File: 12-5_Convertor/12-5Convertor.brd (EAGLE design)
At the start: 29.1 x 41.3 mm, 14 parts, among them U1 LM2678

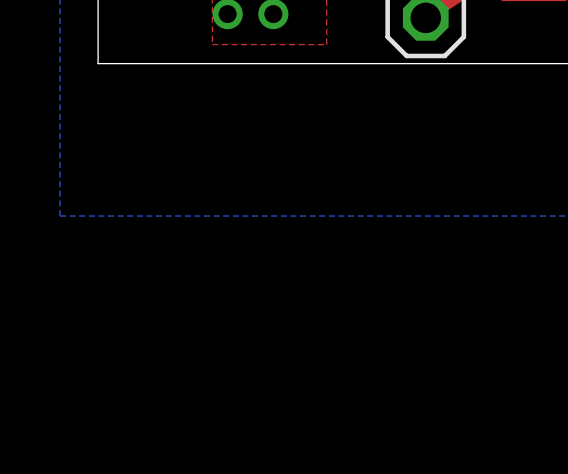
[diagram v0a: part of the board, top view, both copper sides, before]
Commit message: Update the buck regulator.
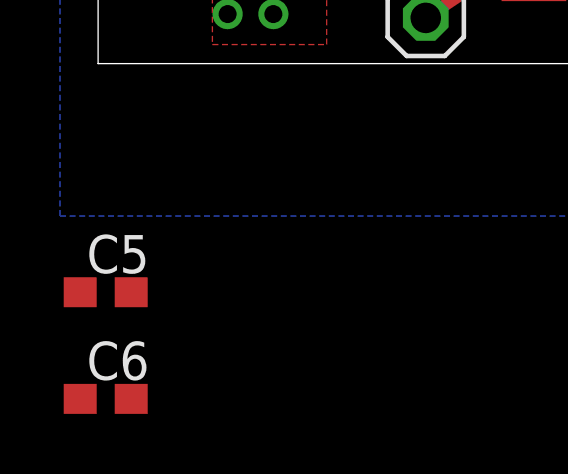
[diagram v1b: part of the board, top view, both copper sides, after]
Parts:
- added C5, C6: (no value), eagle-ltspice:C0603
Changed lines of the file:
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@@
 <?xml version="1.0" encoding="utf-8"?>
 <!DOCTYPE eagle SYSTEM "eagle.dtd">
-<eagle version="7.3.0">
+<eagle version="7.4.0">
 <drawing>
 <settings>
@@
 <attribute name="NAME" x="33.186" y="30.87" size="1.27" layer="21"/>
 </element>
+<element name="C5" library="eagle-ltspice" package="C0603" value="" x="32.004" y="10.16">
+<attribute name="SPICEMODEL" value="NONE" x="32.004" y="10.16" size="1.778" layer="27" display="off"/>
+<attribute name="SPICEPREFIX" value="C" x="32.004" y="10.16" size="1.778" layer="27" display="off"/>
+</element>
+<element name="C6" library="eagle-ltspice" package="C0603" value="" x="32.004" y="6.604">
+<attribute name="SPICEMODEL" value="NONE" x="32.004" y="6.604" size="1.778" layer="27" display="off"/>
+<attribute name="SPICEPREFIX" value="C" x="32.004" y="6.604" size="1.778" layer="27" display="off"/>
+</element>
 </elements>

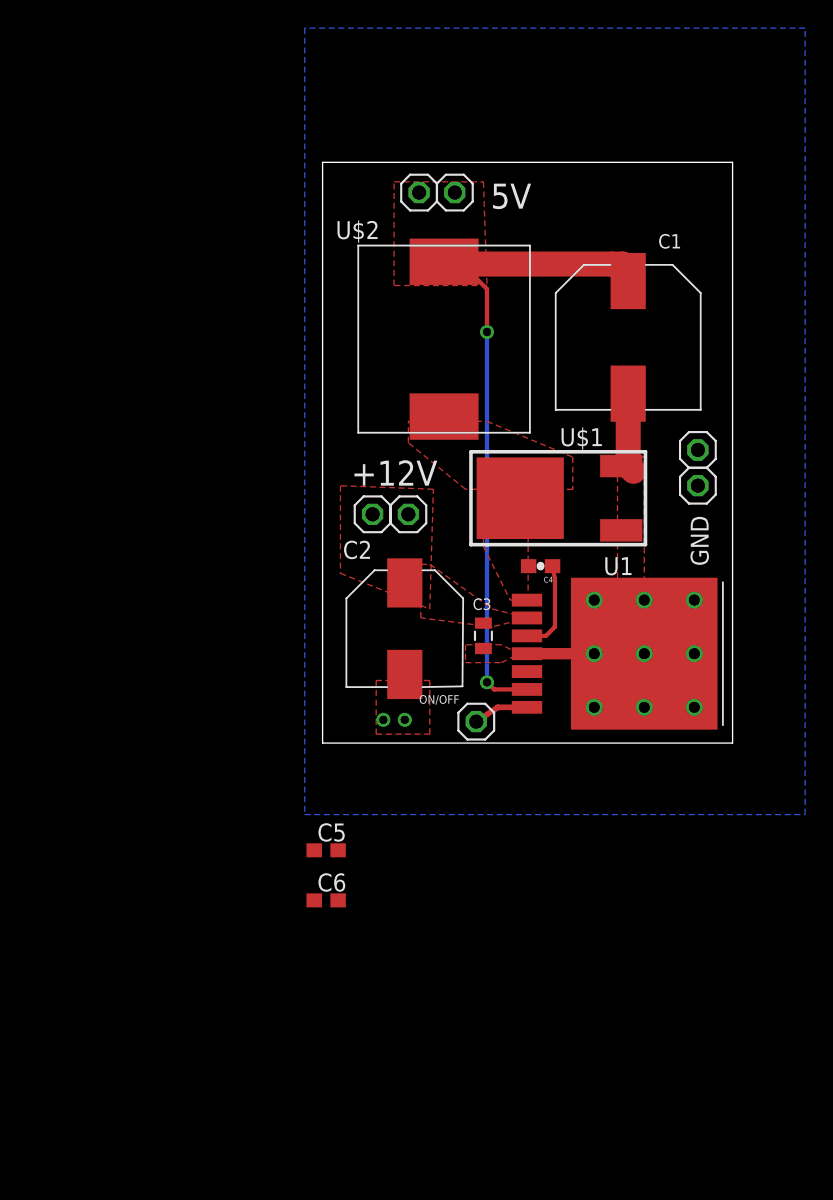
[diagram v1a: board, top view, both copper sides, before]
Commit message: Fixed labels. Added linear regulator and current sensor
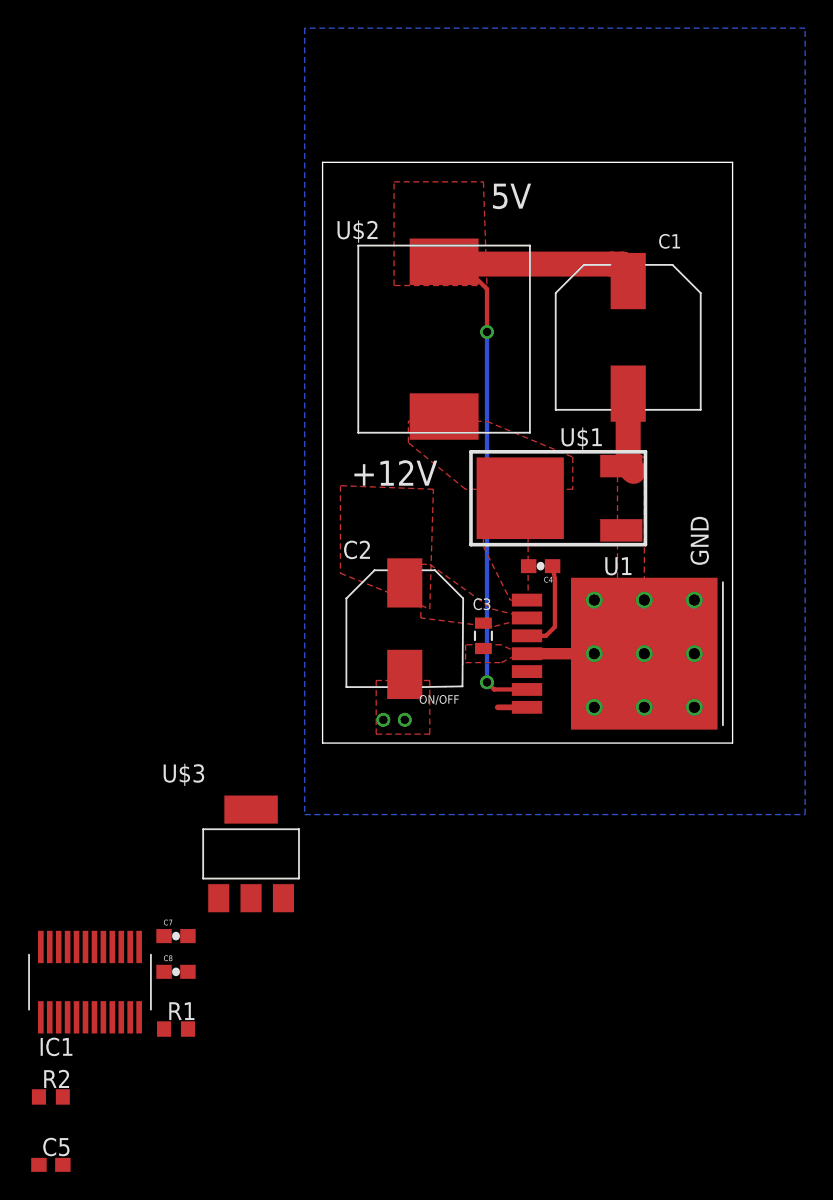
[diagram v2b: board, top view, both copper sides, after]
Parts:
- removed C6: (no value), eagle-ltspice:C0603
- removed JP1, JP2, JP3, JP4, JP5, JP6, JP7: (no value), pinhead:1X01
- added C7, C8: 10UF, SparkFun-Passives:0603-CAP
- added IC1: ACS764, ACS764:SSOP24
- added R1: 1kOhm, DiscreteComponents:R0603
- added R2: 10kOhm, DiscreteComponents:R0603
- added U$3: NCP1117, PowerComponents:NCP1117
- C2: value C-ALUMINUM(47UF) -> 47UF
- C5: value (none) -> 0.1uF
- moved C5 29.7 mm to (12.4, -12.2)
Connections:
- removed net ON/OFF: JP4.1, U1.7
- new net +3V3: C5.1, IC1.8, R1.2, R2.2, U1.7
- new net FAULT: IC1.15, R2.1
- new net N$1: C8.1, R1.1, U$3.OUT
- new net N$10: IC1.14
- new net N$11: IC1.9
- new net N$12: IC1.10
- new net VOUT: C1.+, IC1.1, IC1.2, IC1.3, IC1.4, IC1.5, IC1.6, IC1.7, U$2.P$2
- net +12V: now also C7.1, U$3.INPUT; no longer JP1.1, JP3.1
- net +5V: now also IC1.18, IC1.19, IC1.20, IC1.21, IC1.22, IC1.23, IC1.24; no longer C1.+, JP6.1, JP7.1, U$2.P$2
- net GND: now also C5.2, C7.2, C8.2, IC1.11, IC1.16, IC1.17, U$3.GND; no longer JP2.1, JP5.1
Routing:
- net ON/OFF: track 3.91 -> 0.00 mm
- net +3V3: track 0.00 -> 2.08 mm
- net +5V: track 53.1 -> 52.4 mm
